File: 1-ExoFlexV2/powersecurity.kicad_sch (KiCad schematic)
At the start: 19 parts, among them J1 14 AWG, J2 Jumper, J3 14 AWG, J4 14 AWG, K1 Relay, Q1 MOSFET 20V 200mA, U1 TVS 24V, U2 Shott 100V, U3 Inverter, U4 SR-Latch

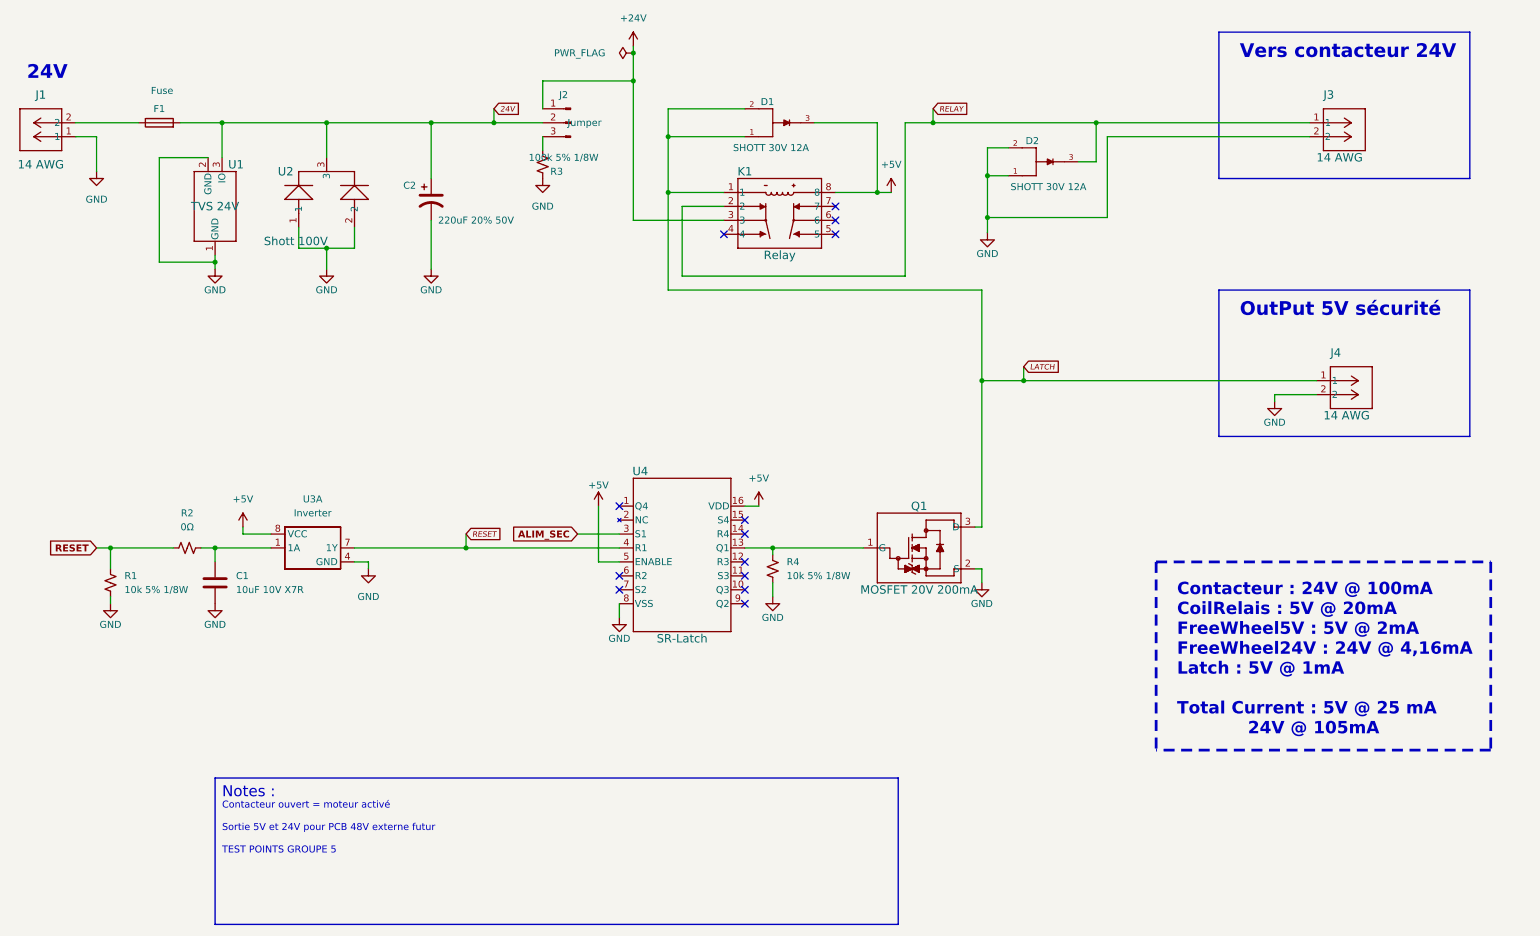
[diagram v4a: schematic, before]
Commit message: Bug NetList
- Ajout de net-tie pour les GND et et les +5V
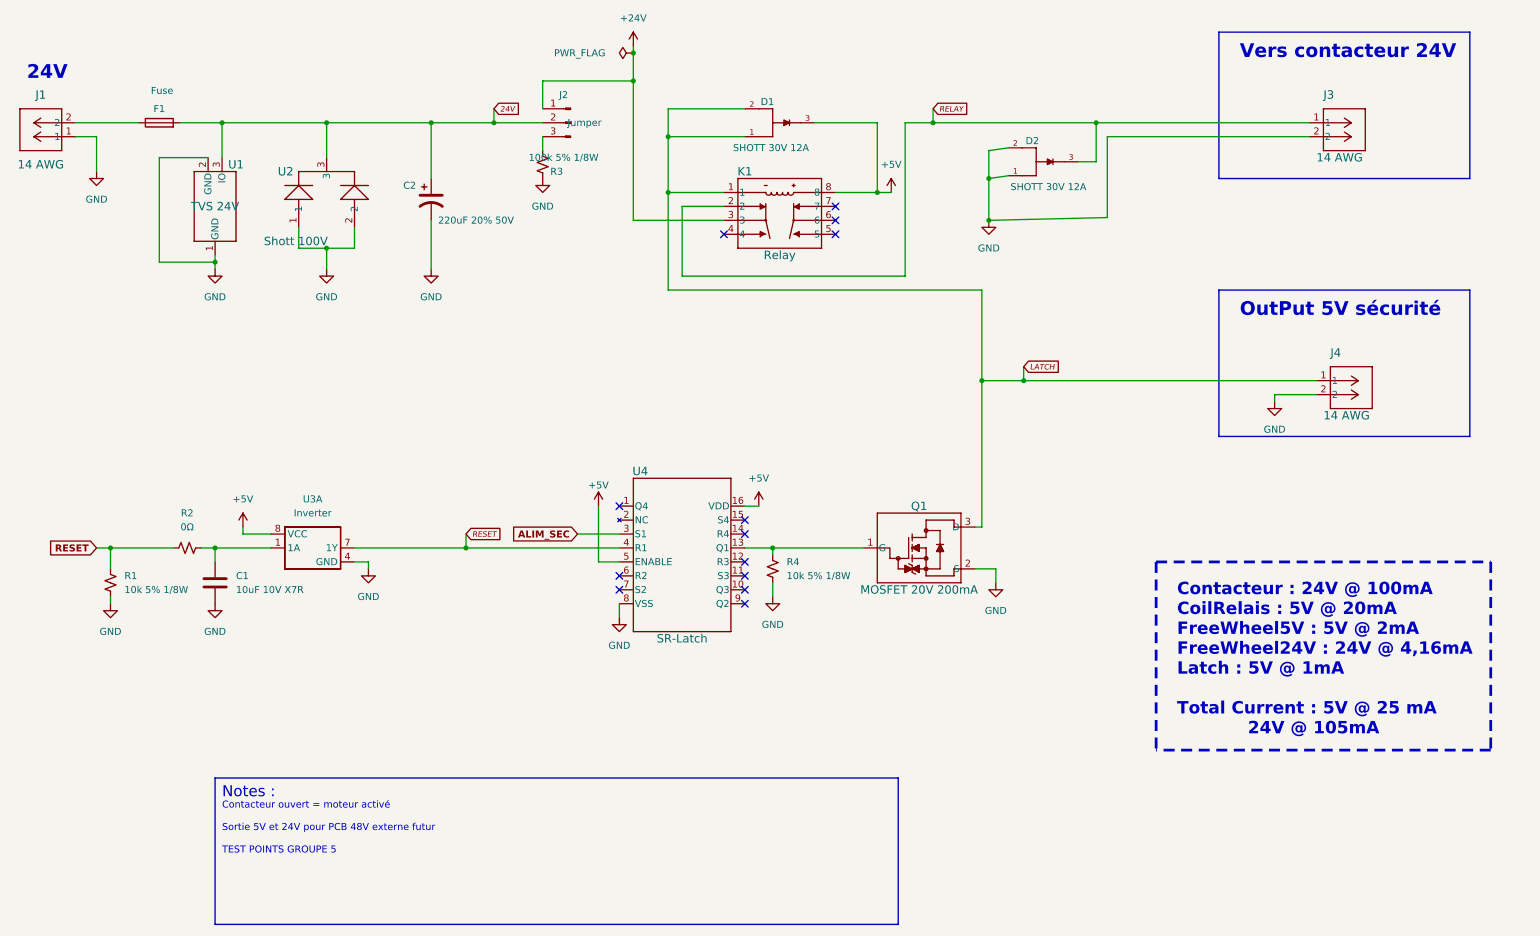
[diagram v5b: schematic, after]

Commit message: Finalisation 3
- Changement des régulateur de tension
- Retrait de test point inutile
- Changement de jumper mal positionner
- Ajout de Mounting holes et fiducial
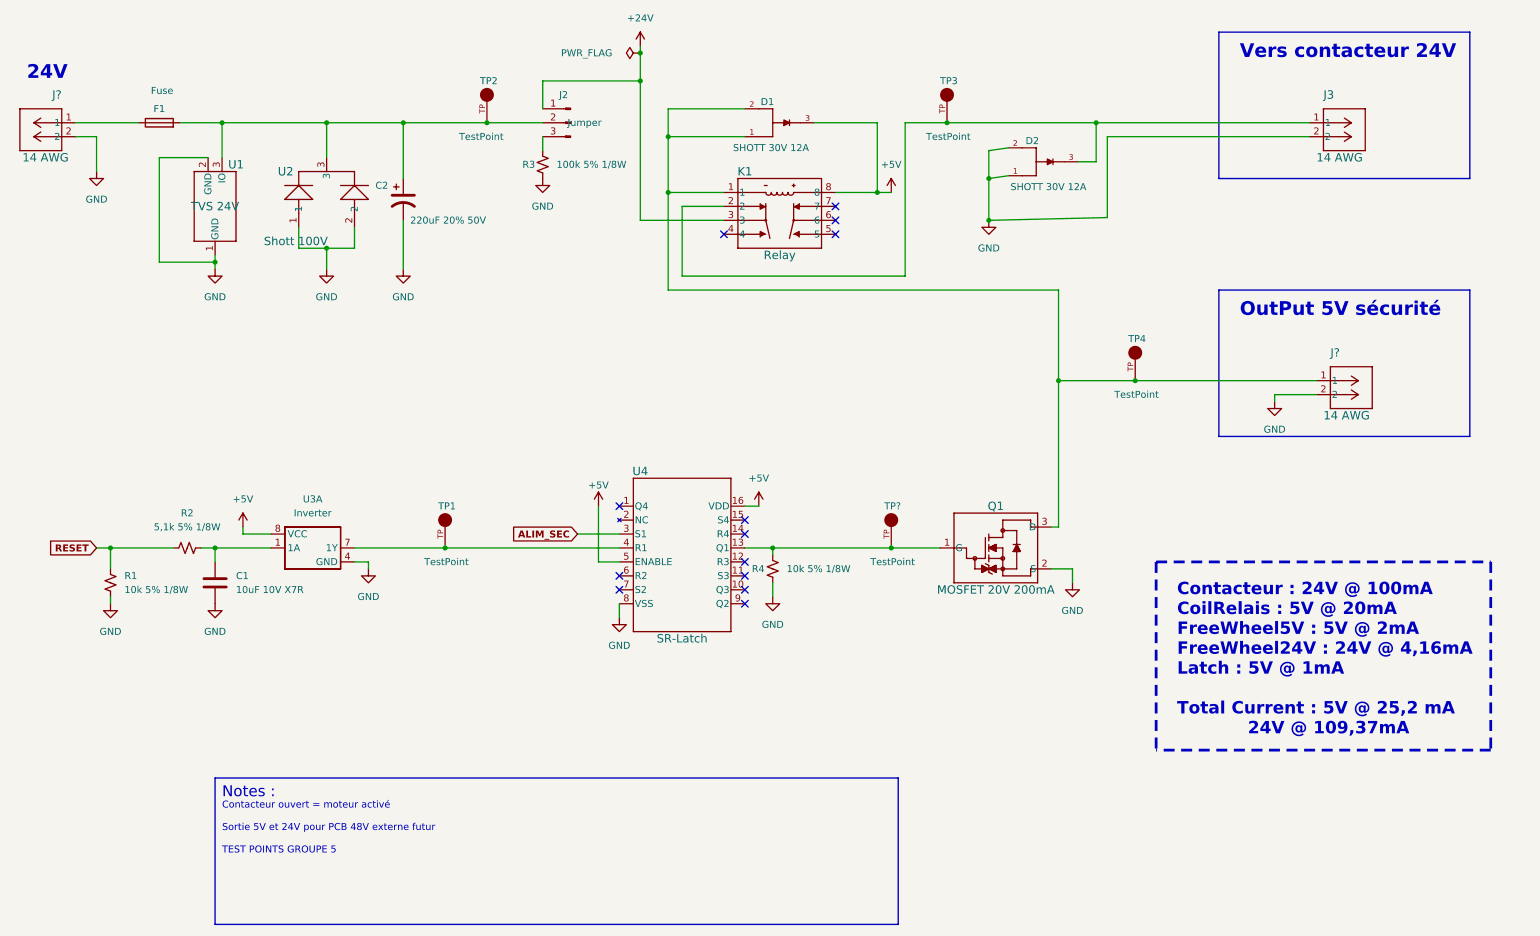
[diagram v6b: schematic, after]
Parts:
- removed J1, J4: 14 AWG, FootPrint:TerminalBlock14AWG, symbol SymLib:1729128
- added J? (x2): 14 AWG, FootPrintLib:PHOENIX_1755736, symbol SymLib:1729128
- added TP1, TP2, TP3, TP4, TP?: TestPoint, FootPrint:KEYSTONE_5005, symbol SymLib:5005
- J2: footprint Connector_PinSocket_2.54mm:PinSocket_1x03_P2.54mm_Vertical -> Connector_PinHeader_2.54mm:PinHeader_1x03_P2.54mm_Vertical
- J3: footprint FootPrint:TerminalBlock14AWG -> FootPrintLib:PHOENIX_1755736; DESCRIPTION 2 Position Wire to Board Terminal Block Horizontal with Boa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 -> 2 Position Terminal Block Header, Male Pins, Shrouded (4 Si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; PART NUMBER 1729128 -> 1755736
- R2: value 0Ω -> 5,1k 5% 1/8W; DESCRIPTION 0 Ohms Jumper Chip Resistor 0805 (2012 Metric) Automotive A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 -> 5.1 kOhms ±5% 0.125W, 1/8W Chip Resistor 0805 (2012 Metric)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; PART NUMBER ERJ-6GEY0R00V -> ERJ-6GEYJ512V
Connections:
- net GND: now also J?.2, J?.2
- net RESET: no longer U3.7 (1Y), U4.4 (R1)
- net at F1.1: now also J?.1
- net at Q1.1 (G), R4.1, U4.13 (Q1): now also TP?.TP
- net 24V: no longer names the net of C2.1, F1.2, J2.2 (Pin_2), U1.3 (IO), U2.3
- net 24V: now also TP2.TP
- net LATCH: no longer names the net of D1.1, D1.2, K1.1, Q1.3 (D)
- net LATCH: now also J?.1, TP4.TP
- net RELAY: no longer names the net of D2.3, J3.1, K1.2
- net RELAY: now also TP3.TP
- new net: TP1.TP, U3.7 (1Y), U4.4 (R1)
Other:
- note added: "Contacteur : 24V @ 100mA CoilRelais : 5V @ 20mA FreeWheel5V : 5V @ 2mA FreeWheel24V : 24V @ 4,16mA Latch : 5V @ 1mA Total Current : 5V @ 25,2 mA 24V @ 109,37mA"
- note removed: "Contacteur : 24V @ 100mA CoilRelais : 5V @ 20mA FreeWheel5V : 5V @ 2mA FreeWheel24V : 24V @ 4,16mA Latch : 5V @ 1mA Total Current : 5V @ 25 mA 24V @ 105mA"
- moved on the sheet: C2, Q1

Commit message: Finalisation schéma FIN
- Changement des uméro pour les inverseurs
- Changement des connecteur et début de placement
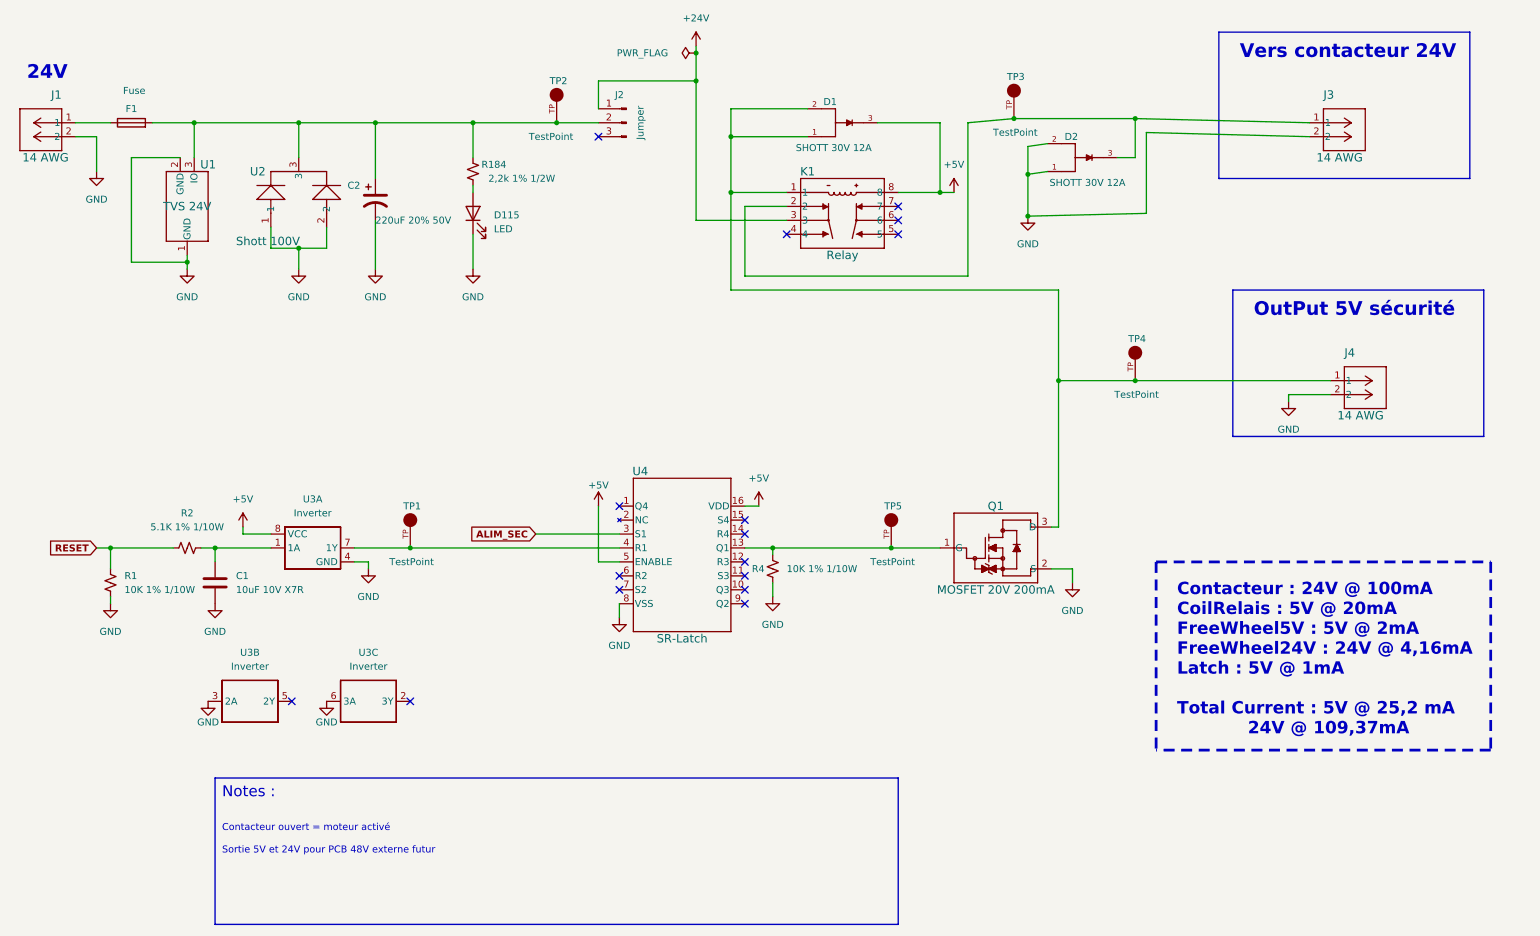
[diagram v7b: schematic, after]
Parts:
- removed R3: 100k 5% 1/8W, Resistor_SMD:R_0805_2012Metric, symbol Device:R_Small_US
- added D115: LED, FootPrintLib:WL-SMCW_0603, symbol Device:LED
- added R184: 2,2k 1% 1/2W, Resistor_SMD:R_0805_2012Metric, symbol Device:R_Small_US
- added unit 3 of U3
- added unit 2 of U3
- F1: PACKAGE 1 Circuit Cartridge -> 5mm x 20mm
- R1, R4: value 10k 5% 1/8W -> 10K 1% 1/10W; footprint Resistor_SMD:R_0805_2012Metric -> Resistor_SMD:R_0603_1608Metric; DESCRIPTION 10 kOhms ±5% 0.125W, 1/8W Chip Resistor 0805 (2012 Metric) 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 -> 10 kOhms ±1% 0.1W, 1/10W Chip Resistor 0603 (1608 Metric) A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; PACKAGE 0805 (2012 Metric) -> 0603 (1608 Metric); PART NUMBER ERJ-6GEYJ103V -> ERJ-3EKF1002V
- R2: value 5,1k 5% 1/8W -> 5.1K 1% 1/10W; footprint Resistor_SMD:R_0805_2012Metric -> Resistor_SMD:R_0603_1608Metric; DESCRIPTION 5.1 kOhms ±5% 0.125W, 1/8W Chip Resistor 0805 (2012 Metric)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 -> 5.1 kOhms ±1% 0.1W, 1/10W Chip Resistor 0603 (1608 Metric) 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; PACKAGE 0805 (2012 Metric) -> 0603 (1608 Metric); PART NUMBER ERJ-6GEYJ512V -> ERJ-3EKF5101V
- TP1, TP2, TP3, TP4: NOTES (none) -> DO NOT POPULATE; PURCHASE-URL https://pricing.snapeda.com/search/part/5005/?ref=eda -> (none)
- TP5: renamed from TP?; NOTES (none) -> DO NOT POPULATE; PURCHASE-URL https://pricing.snapeda.com/search/part/5005/?ref=eda -> (none)
- gave numbers to parts that had none: 2
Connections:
- net GND: now also D115.1 (K), U3.3 (2A), U3.6 (3A)
- net at C2.1, F1.2, J2.2 (Pin_2)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: now also R184.2
- new net: D115.2 (A), R184.1
- no-connect marks 13 -> 16
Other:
- note added: "Contacteur ouvert = moteur activé Sortie 5V et 24V pour PCB 48V externe futur"
- note removed: "Contacteur ouvert = moteur activé Sortie 5V et 24V pour PCB 48V externe futur TEST POINTS GROUPE 5"
- moved on the sheet: C2, D1, D2, F1, J2, J4, K1, TP1, TP2, TP3, U1, U2
